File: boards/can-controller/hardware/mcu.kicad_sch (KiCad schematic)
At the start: 33 parts, among them J1 RPi_GPIO, J2 ICSP, J3 UART, J4 USB-C, U1 PIC32MK1024MCM064-I/PT, U2 MCP1826S-3302E/DB, U3 USBLC6-2SC6, Y1 12MHz

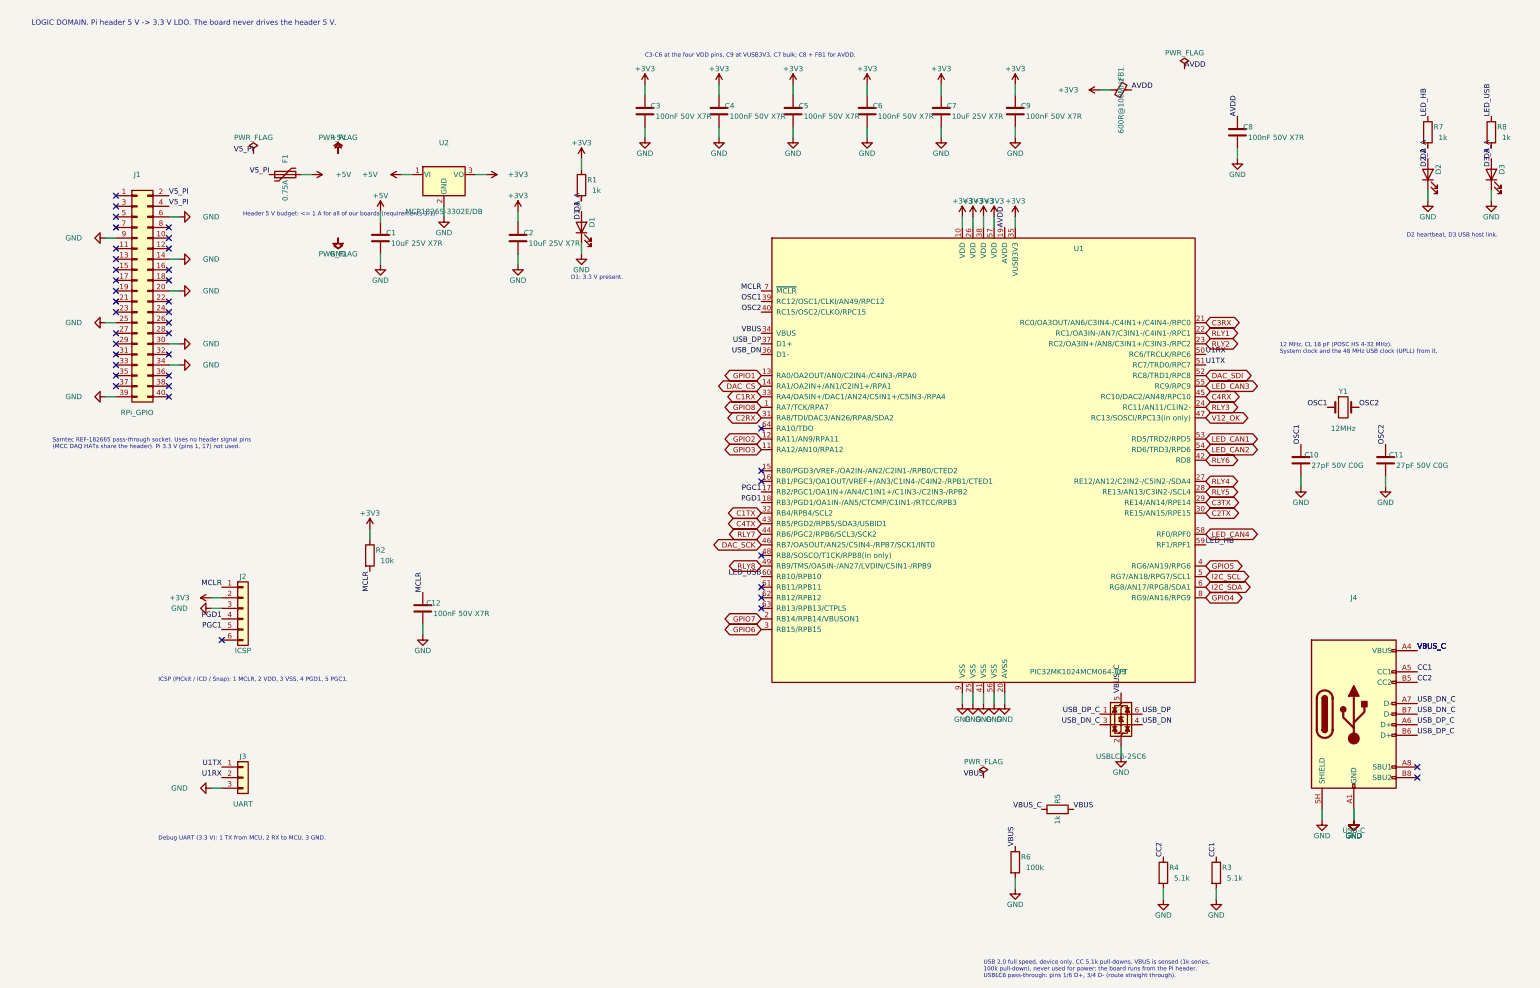
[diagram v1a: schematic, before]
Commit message: can-controller: placement rev 3 so the MCU can fan out, routing WIP
Schematic:
- U1 pin map redone for the MCU rotated 90 deg: each side carries the
  signals for the parts it faces, in order (GPIO left, CAN right, USB /
  crystal / ICSP / UART top, DAC SPI4 / I2C1 bottom). ICSP on PGx2
  (pins 43/44, ICESEL = PGx2), UART1 on 46/47, V12_OK on pin 33.
- Relays driven over I2C1 by an MCP23008 (U33, 0x20); relay channel
  order permuted so expander -> ISO6740 -> ULN2803A -> J30 runs straight
- FB1 removed, AVDD tied to +3V3 (sits between two CAN pin pairs)
- J50 pinout: 1-2 AO1/AO2, 3-6 AI1-4 (outputs no longer cross inputs)
- Interface_Expansion:MCP23008-xSO imported to lib/

PCB:
- place_rev3.py: U1 rotated at (148,131), expander under it, relay
  isolators across the 12 V block's top edge (corner now x = 134),
  ULN below, 12 V opto at the top of the CAN strip, analog section
  re-laid around the new J50 pinout; bottom zones follow the new corner
- Routed: MCU escape nets first, signals top only, then power; 8
  connections open, ~48 clearance near-misses to clean up by hand,
  ~370 mm bottom traces

Co-Authored-By: Claude Opus 5.5 <noreply@anthropic.com>
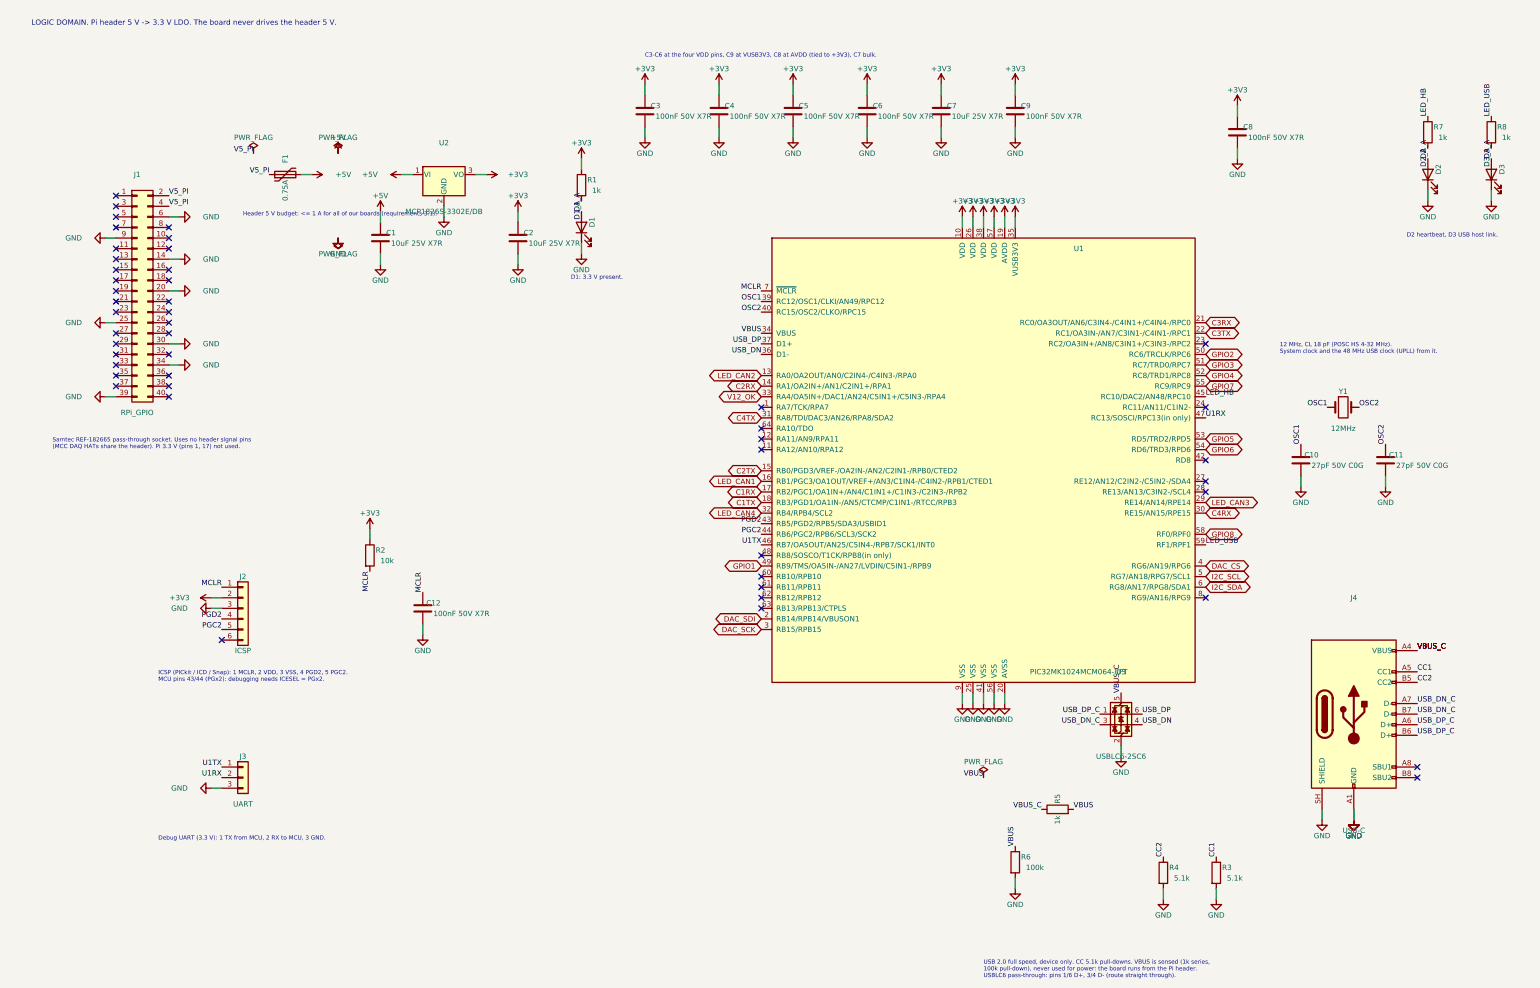
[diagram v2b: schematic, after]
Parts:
- removed FB1: 600R@100MHz, Inductor_SMD:L_0805_2012Metric_Pad1.05x1.20mm_HandSolder, symbol Device:FerriteBead_Small
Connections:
- net AVDD is gone; now on net +3V3: C8.1, U1.19 (AVDD)
- net RLY1 is gone; now on net C3TX: U1.22 (RC1/OA3IN-/AN7/C3IN1-/C4IN1-/RPC1)
- net RLY7 is gone; now on net PGC2: U1.44 (RB6/PGC2/RPB6/SCL3/SCK2)
- net RLY8 is gone; now on net GPIO1: U1.49 (RB9/TMS/OA5IN-/AN27/LVDIN/C5IN1-/RPB9)
- net C1RX: now also U1.17 (RB2/PGC1/OA1IN+/AN4/C1IN1+/C1IN3-/C2IN3-/RPB2); no longer U1.33 (RA4/OA5IN+/DAC1/AN24/C5IN1+/C5IN3-/RPA4)
- net C1TX: now also U1.18 (RB3/PGD1/OA1IN-/AN5/CTCMP/C1IN1-/RTCC/RPB3); no longer U1.32 (RB4/RPB4/SCL2)
- net C2RX: now also U1.14 (RA1/OA2IN+/AN1/C2IN1+/RPA1); no longer U1.31 (RA8/TDI/DAC3/AN26/RPA8/SDA2)
- net C2TX: now also U1.15 (RB0/PGD3/VREF-/OA2IN-/AN2/C2IN1-/RPB0/CTED2); no longer U1.30 (RE15/AN15/RPE15)
- net C3TX: no longer U1.29 (RE14/AN14/RPE14)
- net C4RX: now also U1.30 (RE15/AN15/RPE15); no longer U1.45 (RC10/DAC2/AN48/RPC10)
- net C4TX: now also U1.31 (RA8/TDI/DAC3/AN26/RPA8/SDA2); no longer U1.43 (RB5/PGD2/RPB5/SDA3/USBID1)
- net DAC_CS: now also U1.4 (RG6/AN19/RPG6); no longer U1.14 (RA1/OA2IN+/AN1/C2IN1+/RPA1)
- net DAC_SCK: now also U1.3 (RB15/RPB15); no longer U1.46 (RB7/OA5OUT/AN25/C5IN4-/RPB7/SCK1/INT0)
- net DAC_SDI: now also U1.2 (RB14/RPB14/VBUSON1); no longer U1.52 (RC8/TRD1/RPC8)
- net GPIO1: no longer U1.13 (RA0/OA2OUT/AN0/C2IN4-/C4IN3-/RPA0)
- net GPIO2: now also U1.50 (RC6/TRCLK/RPC6); no longer U1.12 (RA11/AN9/RPA11)
- net GPIO3: now also U1.51 (RC7/TRD0/RPC7); no longer U1.11 (RA12/AN10/RPA12)
- net GPIO4: now also U1.52 (RC8/TRD1/RPC8); no longer U1.8 (RG9/AN16/RPG9)
- net GPIO5: now also U1.53 (RD5/TRD2/RPD5); no longer U1.4 (RG6/AN19/RPG6)
- net GPIO6: now also U1.54 (RD6/TRD3/RPD6); no longer U1.3 (RB15/RPB15)
- net GPIO7: now also U1.55 (RC9/RPC9); no longer U1.2 (RB14/RPB14/VBUSON1)
- net GPIO8: now also U1.58 (RF0/RPF0); no longer U1.1 (RA7/TCK/RPA7)
- net LED_CAN1: now also U1.16 (RB1/PGC3/OA1OUT/VREF+/AN3/C1IN4-/C4IN2-/RPB1/CTED1); no longer U1.53 (RD5/TRD2/RPD5)
- net LED_CAN2: now also U1.13 (RA0/OA2OUT/AN0/C2IN4-/C4IN3-/RPA0); no longer U1.54 (RD6/TRD3/RPD6)
- net LED_CAN3: now also U1.29 (RE14/AN14/RPE14); no longer U1.55 (RC9/RPC9)
- net LED_CAN4: now also U1.32 (RB4/RPB4/SCL2); no longer U1.58 (RF0/RPF0)
- net LED_HB: now also U1.45 (RC10/DAC2/AN48/RPC10); no longer U1.59 (RF1/RPF1)
- net LED_USB: now also U1.59 (RF1/RPF1); no longer U1.60 (RB10/RPB10)
- net U1RX: now also U1.47 (RC13/SOSCI/RPC13(in only)); no longer U1.50 (RC6/TRCLK/RPC6)
- net U1TX: now also U1.46 (RB7/OA5OUT/AN25/C5IN4-/RPB7/SCK1/INT0); no longer U1.51 (RC7/TRD0/RPC7)
- net V12_OK: now also U1.33 (RA4/OA5IN+/DAC1/AN24/C5IN1+/C5IN3-/RPA4); no longer U1.47 (RC13/SOSCI/RPC13(in only))
- net PGC1 renamed PGC2
- net PGC2: no longer U1.17 (RB2/PGC1/OA1IN+/AN4/C1IN1+/C1IN3-/C2IN3-/RPB2)
- net PGD1 renamed PGD2
- net PGD2: now also U1.43 (RB5/PGD2/RPB5/SDA3/USBID1); no longer U1.18 (RB3/PGD1/OA1IN-/AN5/CTCMP/C1IN1-/RTCC/RPB3)
- net RLY2: no longer names the net of U1.23 (RC2/OA3IN+/AN8/C3IN1+/C3IN3-/RPC2)
- net RLY3: no longer names the net of U1.24 (RC11/AN11/C1IN2-)
- net RLY4: no longer names the net of U1.27 (RE12/AN12/C2IN2-/C5IN2-/SDA4)
- net RLY5: no longer names the net of U1.28 (RE13/AN13/C3IN2-/SCL4)
- net RLY6: no longer names the net of U1.42 (RD8)
- no-connect marks 40 -> 48
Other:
- note added: "C3-C6 at the four VDD pins, C9 at VUSB3V3, C8 at AVDD (tied to +3V3), C7 bulk."
- note added: "ICSP (PICkit / ICD / Snap): 1 MCLR, 2 VDD, 3 VSS, 4 PGD2, 5 PGC2. MCU pins 43/44 (PGx2): debugging needs ICESEL = PGx2."
- note removed: "C3-C6 at the four VDD pins, C9 at VUSB3V3, C7 bulk; C8 + FB1 for AVDD."
- note removed: "ICSP (PICkit / ICD / Snap): 1 MCLR, 2 VDD, 3 VSS, 4 PGD1, 5 PGC1."

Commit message: can-controller: schematic for the new scope (Ethernet W6100, 4 x ISOW1044, AQW212 relays, diff AI)
Six sheets generated by gen_schematic.py: MCU and logic power, Ethernet,
CAN x4, 12 V input and isolated logic supply (TDN 5-2411WI), relay drive,
GPIO and analog in. ERC 0; netlist check: no net crosses a domain except
at the designed crossings. New lib parts: Thl_Interface:W6100-L (flat),
Thl_Isolator:AQW212, stock ISOW1044 / TDN 5WI / LQFP-48 / bead footprints.
PCB still holds the old layout (next: update from schematic, placement).

Co-Authored-By: Claude Opus 5.5 <noreply@anthropic.com>
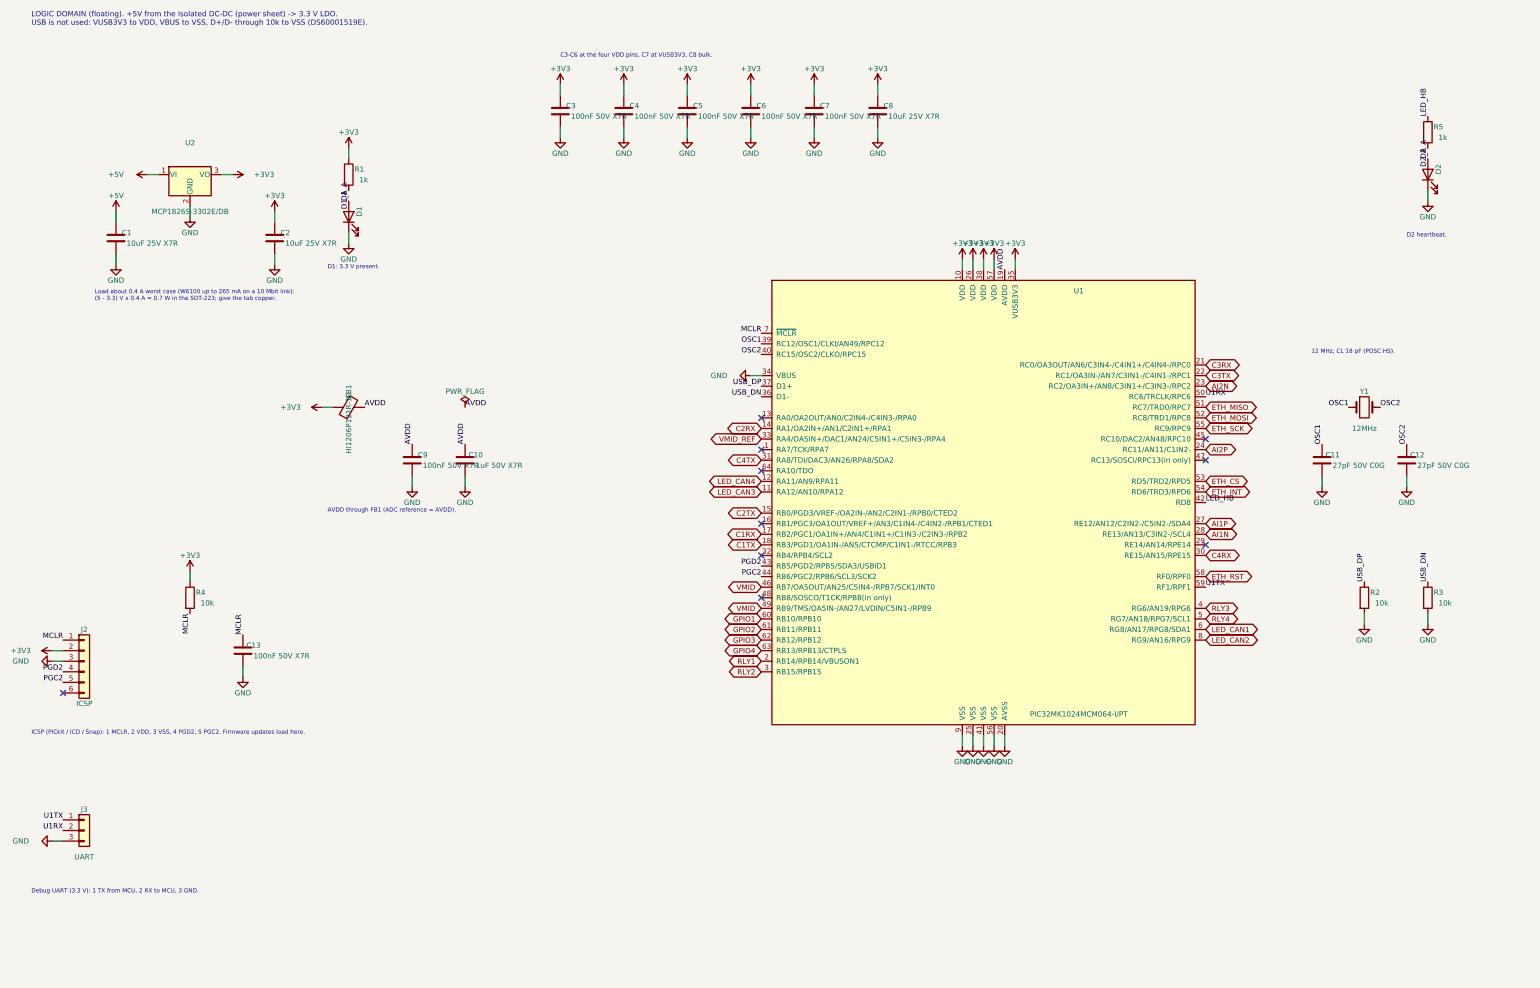
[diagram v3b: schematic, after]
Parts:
- removed D3: LED green, LED_SMD:LED_1206_3216Metric_Pad1.42x1.75mm_HandSolder, symbol Device:LED
- removed F1: 0.75A, Fuse:Fuse_1206_3216Metric_Pad1.42x1.75mm_HandSolder, symbol Device:Polyfuse
- removed J1: RPi_GPIO, Thl_Connector:Samtec_REF-182665_2x20_P2.54mm_PassThrough, symbol Connector_Generic:Conn_02x20_Odd_Even
- removed J4: USB-C, Connector_USB:USB_C_Receptacle_GCT_USB4085, symbol Connector:USB_C_Receptacle_USB2.0_16P
- removed R6: 100k, Resistor_SMD:R_1206_3216Metric_Pad1.30x1.75mm_HandSolder, symbol Device:R
- removed R7, R8: 1k, Resistor_SMD:R_1206_3216Metric_Pad1.30x1.75mm_HandSolder, symbol Device:R
- removed U3: USBLC6-2SC6, Package_TO_SOT_SMD:SOT-23-6, symbol Power_Protection:USBLC6-2P6
- added C13: 100nF 50V X7R, Capacitor_SMD:C_0805_2012Metric_Pad1.18x1.45mm_HandSolder, symbol Device:C
- added FB1: HI1206P121R-10, Inductor_SMD:L_1206_3216Metric_Pad1.22x1.90mm_HandSolder, symbol Device:FerriteBead
- C10: value 27pF 50V C0G -> 1uF 50V X7R; footprint Capacitor_SMD:C_0805_2012Metric_Pad1.18x1.45mm_HandSolder -> Capacitor_SMD:C_1206_3216Metric_Pad1.33x1.80mm_HandSolder; MPN GRM2165C1H270JA01D -> GRM31MR71H105KA88L
- C12: value 100nF 50V X7R -> 27pF 50V C0G; MPN GRM21BR71H104KA01L -> GRM2165C1H270JA01D
- C7: value 10uF 25V X7R -> 100nF 50V X7R; footprint Capacitor_SMD:C_1206_3216Metric_Pad1.33x1.80mm_HandSolder -> Capacitor_SMD:C_0805_2012Metric_Pad1.18x1.45mm_HandSolder; MPN GRM31CR71E106KA12L -> GRM21BR71H104KA01L
- C8: value 100nF 50V X7R -> 10uF 25V X7R; footprint Capacitor_SMD:C_0805_2012Metric_Pad1.18x1.45mm_HandSolder -> Capacitor_SMD:C_1206_3216Metric_Pad1.33x1.80mm_HandSolder; MPN GRM21BR71H104KA01L -> GRM31CR71E106KA12L
- R3, R4: value 5.1k -> 10k; MPN RC1206FR-075K1L -> RC1206FR-0710KL
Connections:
- net CC1 is gone; now on net USB_DN: R3.1
- net CC2 is gone; now on net +3V3: R4.1
- net I2C_SDA is gone; now on net LED_CAN1: U1.6 (RG8/AN17/RPG8/SDA1)
- net LED_USB is gone; now on net U1TX: U1.59 (RF1/RPF1)
- net VBUS_C is gone; now on net LED_HB: R5.1
- net +3V3: now also FB1.1; no longer C9.1, R2.1, U1.19 (AVDD)
- net D2_A: now also R5.2
- net GND: now also R2.2, U1.34 (VBUS), C13.2; no longer R4.2
- net GPIO1: now also U1.60 (RB10/RPB10); no longer U1.49 (RB9/TMS/OA5IN-/AN27/LVDIN/C5IN1-/RPB9)
- net GPIO2: now also U1.61 (RB11/RPB11); no longer U1.50 (RC6/TRCLK/RPC6)
- net GPIO3: now also U1.62 (RB12/RPB12); no longer U1.51 (RC7/TRD0/RPC7)
- net GPIO4: now also U1.63 (RB13/RPB13/CTPLS); no longer U1.52 (RC8/TRD1/RPC8)
- net LED_CAN1: no longer U1.16 (RB1/PGC3/OA1OUT/VREF+/AN3/C1IN4-/C4IN2-/RPB1/CTED1)
- net LED_CAN2: now also U1.8 (RG9/AN16/RPG9); no longer U1.13 (RA0/OA2OUT/AN0/C2IN4-/C4IN3-/RPA0)
- net LED_CAN3: now also U1.11 (RA12/AN10/RPA12); no longer U1.29 (RE14/AN14/RPE14)
- net LED_CAN4: now also U1.12 (RA11/AN9/RPA11); no longer U1.32 (RB4/RPB4/SCL2)
- net LED_HB: now also U1.42 (RD8); no longer U1.45 (RC10/DAC2/AN48/RPC10)
- net MCLR: now also R4.2, C13.1; no longer C12.1, R2.2
- net OSC1: now also C11.1; no longer C10.1
- net OSC2: now also C12.1; no longer C11.1
- net U1RX: now also U1.50 (RC6/TRCLK/RPC6); no longer U1.47 (RC13/SOSCI/RPC13(in only))
- net U1TX: no longer U1.46 (RB7/OA5OUT/AN25/C5IN4-/RPB7/SCK1/INT0)
- net USB_DP: now also R2.1
- net AI2N: now reaches U1.23 (RC2/OA3IN+/AN8/C3IN1+/C3IN3-/RPC2)
- net AI2P: now reaches U1.24 (RC11/AN11/C1IN2-)
- net AI1P: now reaches U1.27 (RE12/AN12/C2IN2-/C5IN2-/SDA4)
- net AI1N: now reaches U1.28 (RE13/AN13/C3IN2-/SCL4)
- net DAC_CS renamed RLY3
- net DAC_SCK renamed RLY2
- net DAC_SDI renamed RLY1
- net GPIO5 renamed ETH_CS
- net GPIO6 renamed ETH_INT
- net GPIO7 renamed ETH_SCK
- net GPIO8 renamed ETH_RST
- net I2C_SCL renamed RLY4
- net V12_OK renamed VMID_REF
- removed net VBUS: R5.2, U1.34 (VBUS)
- new net AVDD: C10.1, C9.1, FB1.2, U1.19 (AVDD)
- new net ETH_MISO: U1.51 (RC7/TRD0/RPC7)
- new net ETH_MOSI: U1.52 (RC8/TRD1/RPC8)
- new net VMID: U1.46 (RB7/OA5OUT/AN25/C5IN4-/RPB7/SCK1/INT0), U1.49 (RB9/TMS/OA5IN-/AN27/LVDIN/C5IN1-/RPB9)
- no-connect marks 48 -> 10
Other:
- note added: "12 MHz, CL 18 pF (POSC HS)."
- note added: "AVDD through FB1 (ADC reference = AVDD)."
- note added: "C3-C6 at the four VDD pins, C7 at VUSB3V3, C8 bulk."
- note added: "D2 heartbeat."
- note added: "ICSP (PICkit / ICD / Snap): 1 MCLR, 2 VDD, 3 VSS, 4 PGD2, 5 PGC2. Firmware updates load here."
- note added: "LOGIC DOMAIN (floating). +5V from the isolated DC-DC (power sheet) -> 3.3 V LDO. USB is not used: VUSB3V3 to VDD, VBUS to VSS, D+/D- through 10k to VSS (DS60001519E)."
- note added: "Load about 0.4 A worst case (W6100 up to 265 mA on a 10 Mbit link): (5 - 3.3) V x 0.4 A = 0.7 W in the SOT-223; give the tab copper."
- note removed: "12 MHz, CL 18 pF (POSC HS 4-32 MHz). System clock and the 48 MHz USB clock (UPLL) from it."
- note removed: "C3-C6 at the four VDD pins, C9 at VUSB3V3, C8 at AVDD (tied to +3V3), C7 bulk."
- note removed: "D2 heartbeat, D3 USB host link."
- note removed: "Header 5 V budget: <= 1 A for all of our boards (requirements 3.1)."
- note removed: "ICSP (PICkit / ICD / Snap): 1 MCLR, 2 VDD, 3 VSS, 4 PGD2, 5 PGC2. MCU pins 43/44 (PGx2): debugging needs ICESEL = PGx2."
- note removed: "LOGIC DOMAIN. Pi header 5 V -> 3.3 V LDO. The board never drives the header 5 V."
- note removed: "Samtec REF-182665 pass-through socket. Uses no header signal pins (MCC DAQ HATs share the header). Pi 3.3 V (pins 1, 17) not used."
- note removed: "USB 2.0 full speed, device only. CC 5.1k pull-downs. VBUS is sensed (1k series, 100k pull-down), never used for power: the board runs from the Pi header. USBLC6 pass-through: pins 1/6 D+, 3/4 D- (route straight through)."
- title: CAN controller: MCU, USB, logic power -> CAN controller: MCU and logic power
